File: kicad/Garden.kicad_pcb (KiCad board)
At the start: 2 copper layers, 13 parts, among them J1 Conn_01x03, J10 Conn_01x02, J2 Conn_01x03, J3 Conn_01x04, J4 Conn_01x06, J5 Conn_01x02, J6 Conn_01x02, J7 Conn_01x06, J8 Conn_01x03, J9 Conn_01x04

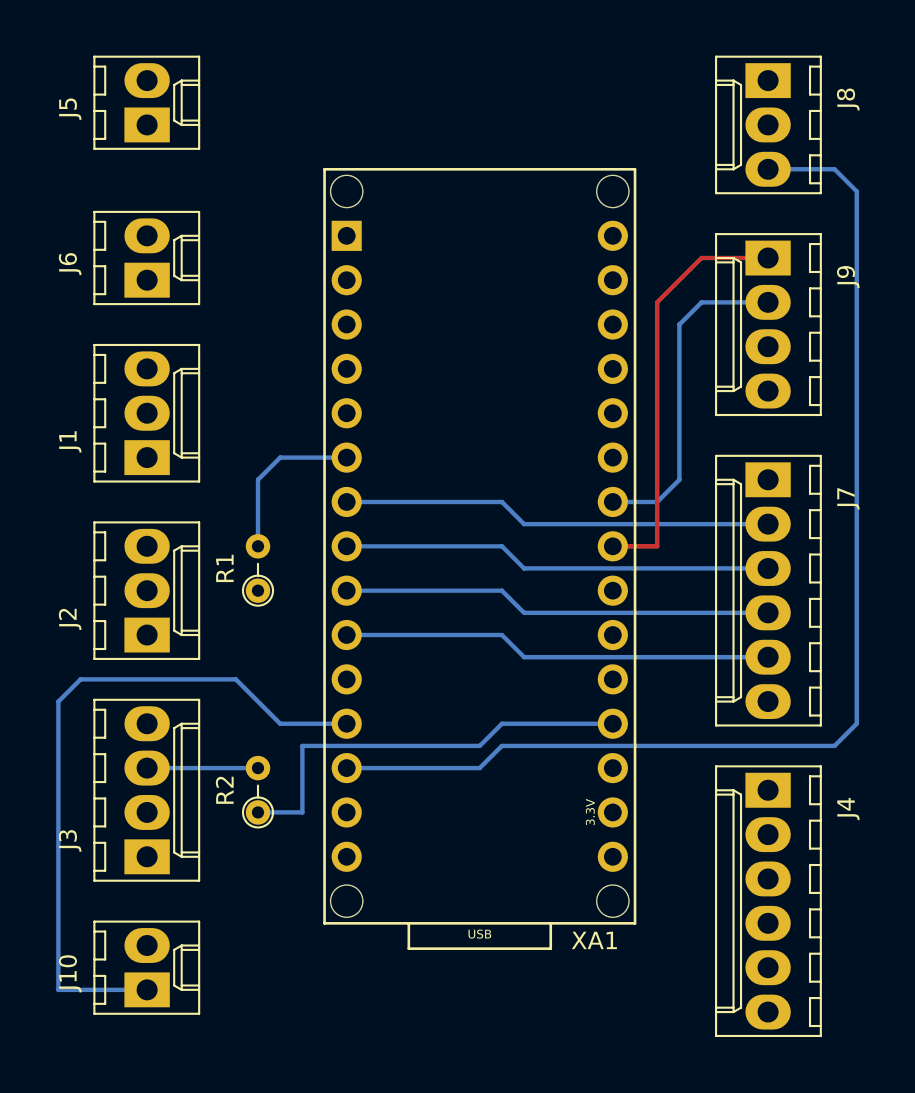
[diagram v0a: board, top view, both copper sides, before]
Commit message: Add connections for serial port to kicad files, add ground and +5V plane
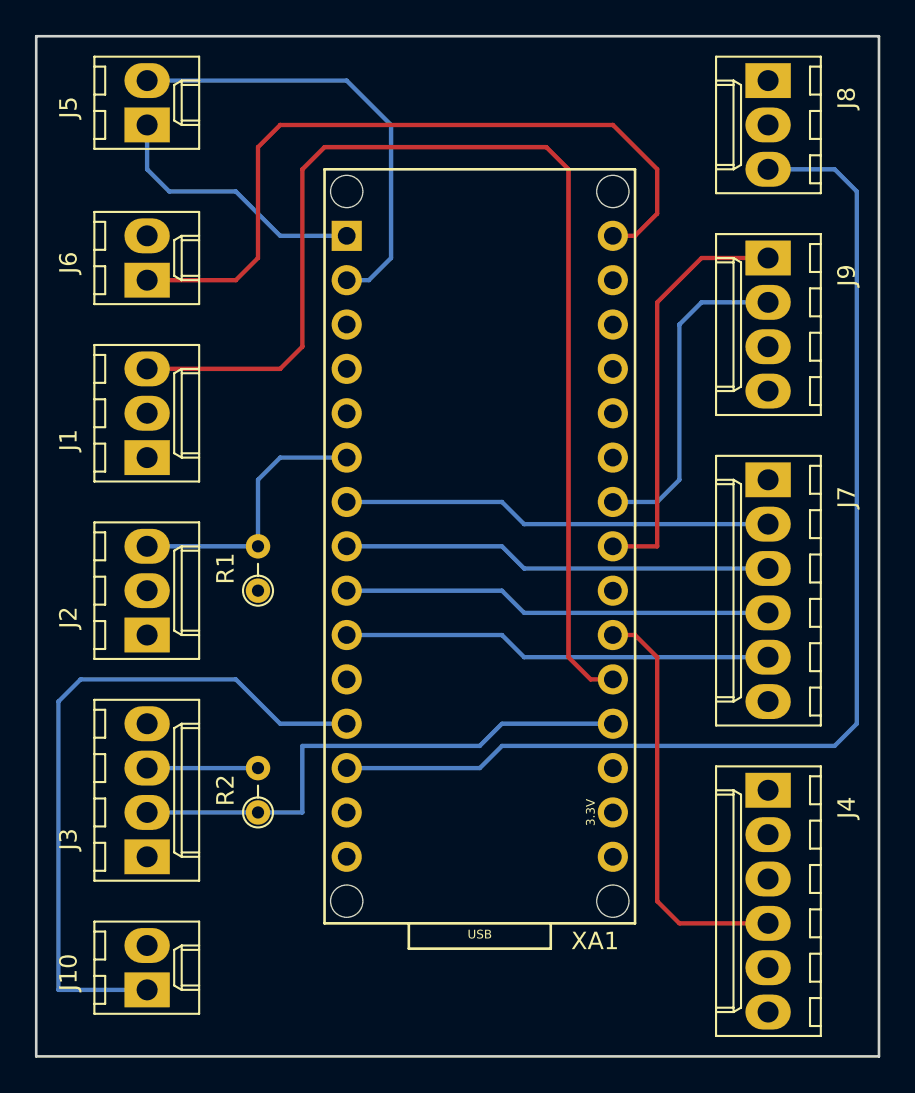
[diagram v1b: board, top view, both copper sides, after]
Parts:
- J1: value Conn_01x03 -> EC
- J10: value Conn_01x02 -> FAN_PWM
- J2: value Conn_01x03 -> TEMP
- J3: value Conn_01x04 -> DHT
- J4: value Conn_01x06 -> PH
- J5: value Conn_01x02 -> Serial
- J6: value Conn_01x02 -> Power
- J7: value Conn_01x06 -> RELAIS
- J8: value Conn_01x03 -> RC
- J9: value Conn_01x04 -> LCD
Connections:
- J4 pad 3: Net-(J4-Pad3) -> GND
- XA1 pad A1: Net-(XA1-PadA1) -> Net-(J1-Pad3)
- XA1 pad A2: Net-(XA1-PadA2) -> Net-(J4-Pad4)
- XA1 pad D0: Net-(XA1-PadD0) -> Net-(J5-Pad2)
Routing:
- net Net-(J1-Pad3): track 0.00 -> 66.9 mm
- net Net-(J6-Pad1): track 0.00 -> 43.3 mm
- net Net-(J5-Pad2): track 0.00 -> 25.7 mm
- net Net-(J4-Pad4): track 0.00 -> 23.9 mm
- net Net-(J5-Pad1): track 0.00 -> 15.5 mm
- net Net-(J3-Pad2): track 24.7 -> 31.0 mm
- net Net-(J2-Pad3): track 9.42 -> 15.8 mm
- added copper zone on F.Cu, net +5V
- added copper zone on B.Cu, net GND
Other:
- board outline added: 48.3 x 58.4 mm

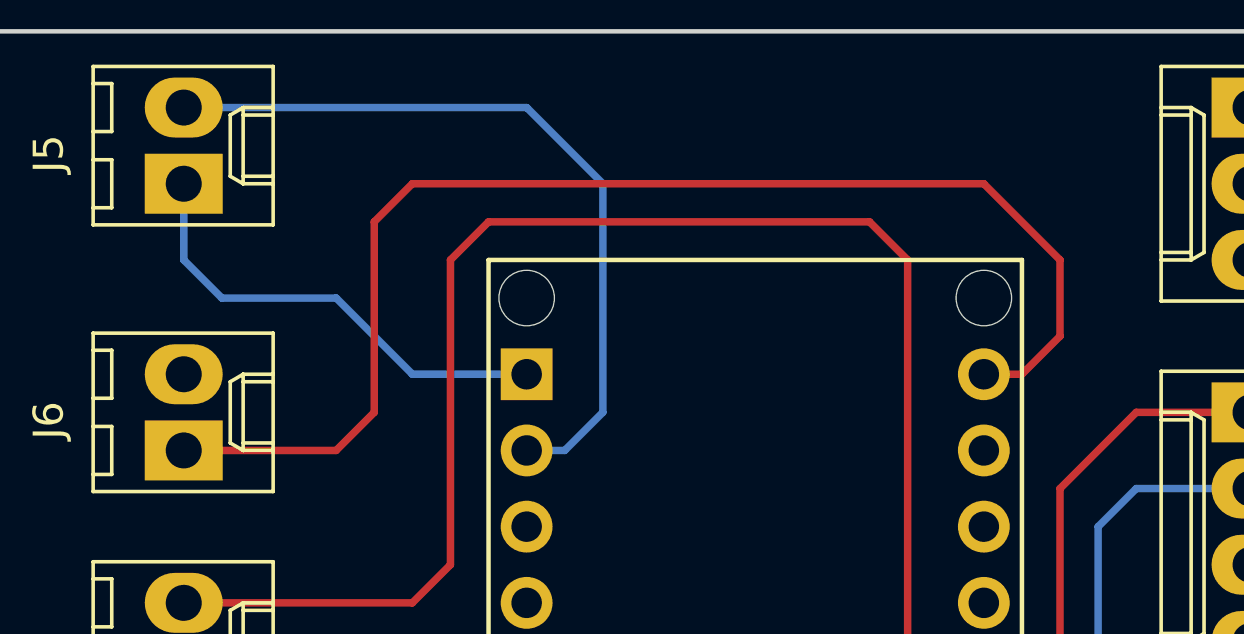
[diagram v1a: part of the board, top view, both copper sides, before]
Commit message: Clean up kicad schematic
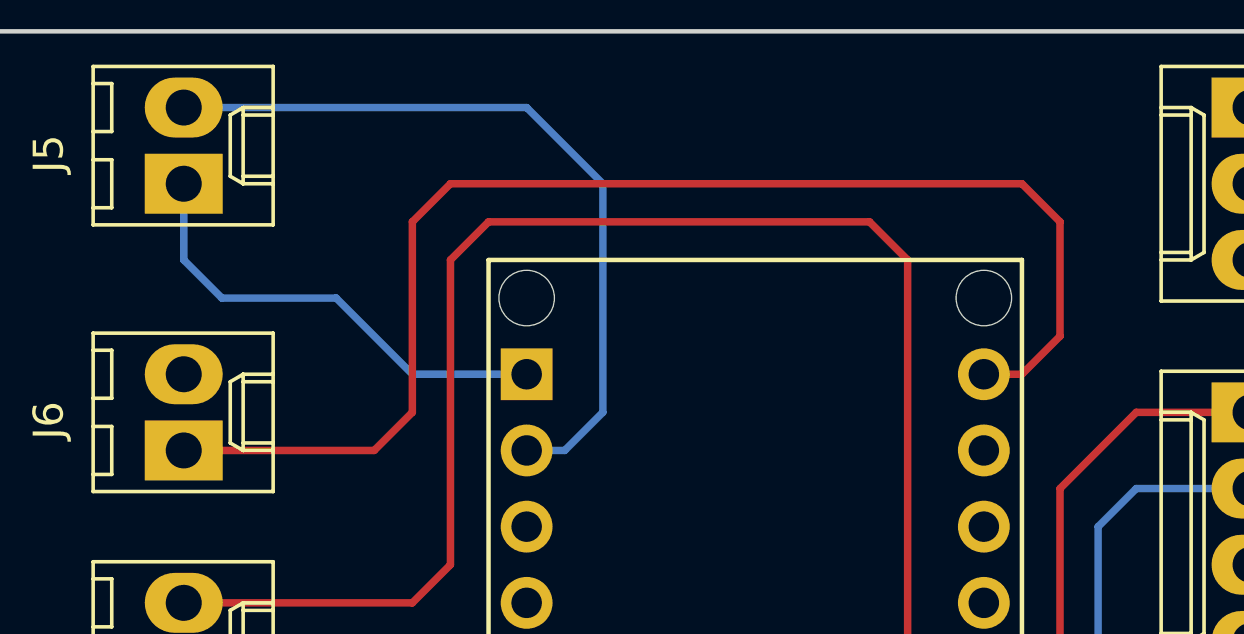
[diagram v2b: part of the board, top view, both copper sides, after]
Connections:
- net Net-(J1-Pad3) renamed A1
- net Net-(J10-Pad1) renamed D9
- net Net-(J2-Pad3) renamed D3
- net Net-(J3-Pad2) renamed A0
- net Net-(J4-Pad4) renamed A2
- net Net-(J5-Pad1) renamed TX
- net Net-(J5-Pad2) renamed RX
- net Net-(J6-Pad1) renamed VCC
- net Net-(J7-Pad2) renamed D4
- net Net-(J7-Pad3) renamed D5
- net Net-(J7-Pad4) renamed D6
- net Net-(J7-Pad5) renamed D7
- net Net-(J8-Pad3) renamed D10
- net Net-(J9-Pad1) renamed A4
- net Net-(J9-Pad2) renamed A5
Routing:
- net VCC: track 43.3 -> 44.0 mm

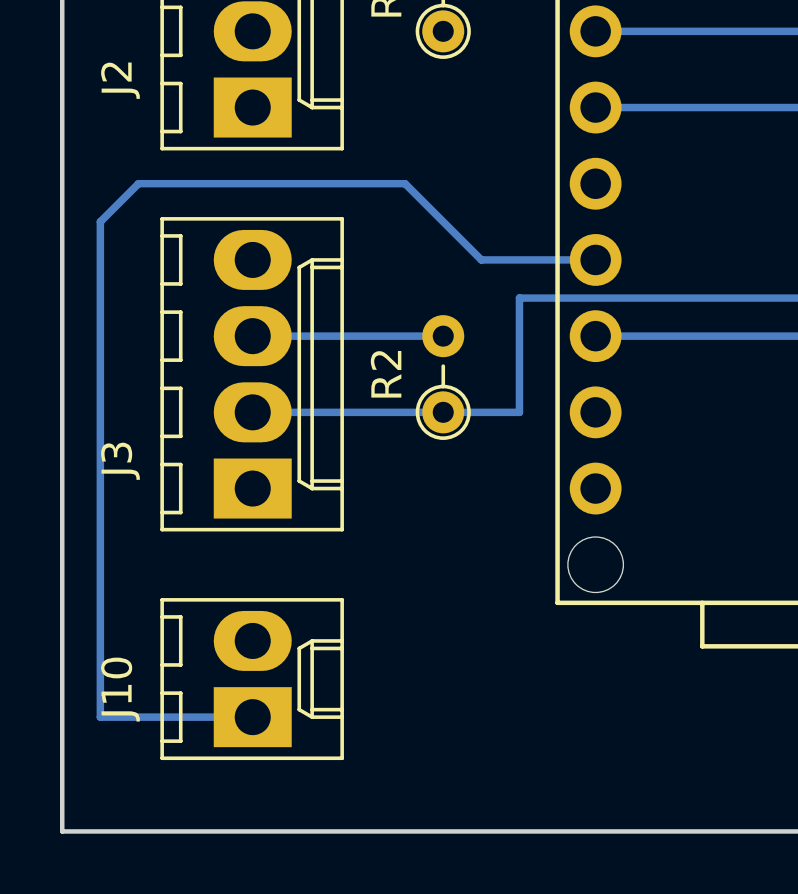
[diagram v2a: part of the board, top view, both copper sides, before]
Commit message: Fix unconnected planes
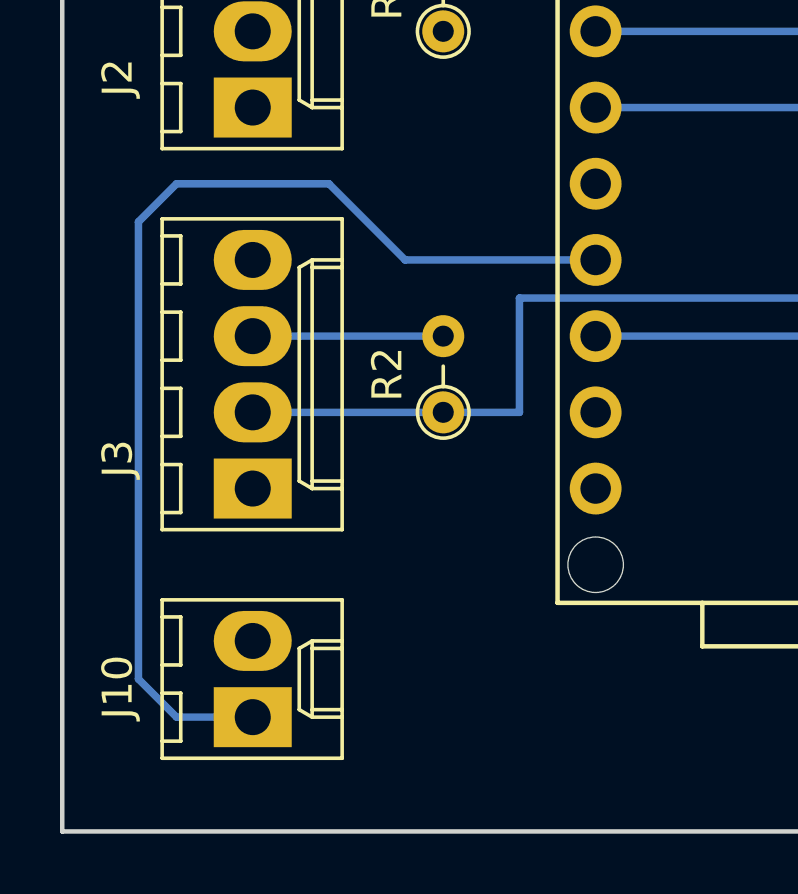
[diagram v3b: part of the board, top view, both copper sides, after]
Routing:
- net D9: track 39.7 -> 36.4 mm
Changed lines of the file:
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@@
   (general
     (links 37)
-    (no_connects 1)
+    (no_connects 0)
     (area 157.404999 78.664999 205.815001 137.235001)
     (thickness 1.6)
     (drawings 4)
-    (tracks 78)
+    (tracks 79)
     (zones 0)
     (modules 13)
@@
   (segment (start 194.31 104.14) (end 194.31 95.25) (width 0.25) (layer B.Cu) (net 31))
   (segment (start 193.04 105.41) (end 194.31 104.14) (width 0.25) (layer B.Cu) (net 31))
-  (segment (start 175.26 118.11) (end 171.45 118.11) (width 0.25) (layer B.Cu) (net 32))
-  (segment (start 158.75 133.35) (end 163.83 133.35) (width 0.25) (layer B.Cu) (net 32))
-  (segment (start 158.75 116.84) (end 158.75 133.35) (width 0.25) (layer B.Cu) (net 32))
-  (segment (start 160.02 115.57) (end 158.75 116.84) (width 0.25) (layer B.Cu) (net 32))
-  (segment (start 168.91 115.57) (end 160.02 115.57) (width 0.25) (layer B.Cu) (net 32))
-  (segment (start 171.45 118.11) (end 168.91 115.57) (width 0.25) (layer B.Cu) (net 32))
+  (segment (start 175.26 118.11) (end 168.91 118.11) (width 0.25) (layer B.Cu) (net 32))
+  (segment (start 161.29 133.35) (end 163.83 133.35) (width 0.25) (layer B.Cu) (net 32))
+  (segment (start 160.02 132.08) (end 161.29 133.35) (width 0.25) (layer B.Cu) (net 32))
+  (segment (start 160.02 116.84) (end 160.02 132.08) (width 0.25) (layer B.Cu) (net 32))
+  (segment (start 161.29 115.57) (end 160.02 116.84) (width 0.25) (layer B.Cu) (net 32))
+  (segment (start 166.37 115.57) (end 161.29 115.57) (width 0.25) (layer B.Cu) (net 32))
+  (segment (start 168.91 118.11) (end 166.37 115.57) (width 0.25) (layer B.Cu) (net 32))
   (zone (net 17) (net_name +5V) (layer F.Cu) (hatch edge 0.508)
     (connect_pads (clearance 0.508))

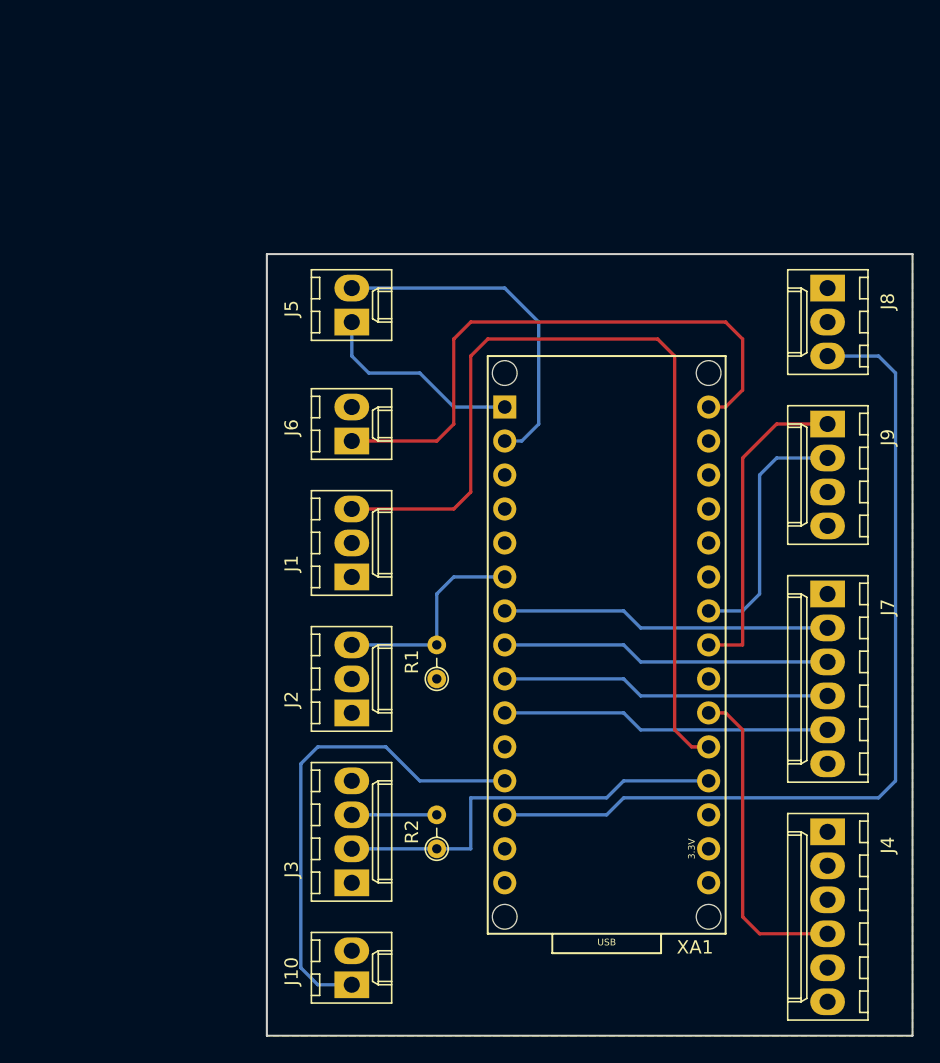
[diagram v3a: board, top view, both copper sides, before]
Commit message: Create Branch with buttons
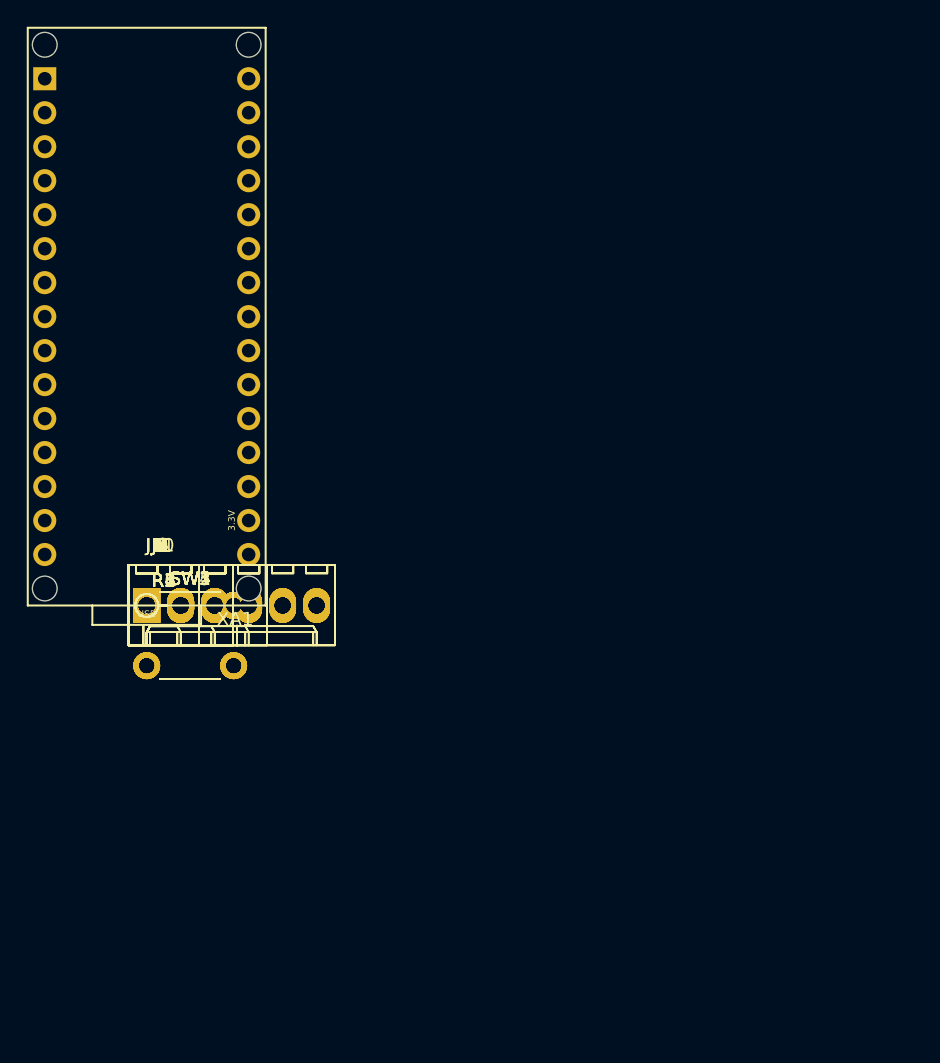
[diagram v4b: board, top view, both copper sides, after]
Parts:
- added J11: SPI, Connectors_Molex:Molex_KK-6410-06_06x2.54mm_Straight, F.Cu at (148.5, 105.0)
- added R3, R4, R5, R6, R7: R, Resistors_THT:R_Axial_DIN0204_L3.6mm_D1.6mm_P2.54mm_Vertical, F.Cu at (148.5, 105.0)
- added SW1, SW2, SW3, SW4, SW5: SW_Push, Buttons_Switches_THT:SW_PUSH_6mm, F.Cu at (148.5, 105.0)
- moved J8 56.1 mm to (148.5, 105.0), turned to 0 degrees
- moved J4 53.6 mm to (148.5, 105.0), turned to 0 degrees
- moved J9 52.7 mm to (148.5, 105.0), turned to 0 degrees
- moved J7 50.9 mm to (148.5, 105.0), turned to 0 degrees
- moved XA1 42.2 mm to (148.5, 105.0)
- moved J10 32.2 mm to (148.5, 105.0), turned to 0 degrees
- moved R2 28.3 mm to (148.5, 105.0), turned to 0 degrees
- moved J5 26.1 mm to (148.5, 105.0), turned to 0 degrees
- moved J3 25.8 mm to (148.5, 105.0), turned to 0 degrees
- moved R1 22.4 mm to (148.5, 105.0), turned to 0 degrees
- moved J6 19.6 mm to (148.5, 105.0), turned to 0 degrees
- moved J2 17.3 mm to (148.5, 105.0), turned to 0 degrees
- moved J1 15.5 mm to (148.5, 105.0), turned to 0 degrees
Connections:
- J8 pad 3: D10 -> D8
- XA1 pad D10: D10 -> D10_CS
- XA1 pad D11: Net-(XA1-PadD11) -> D11_MOSI
- XA1 pad D12: Net-(XA1-PadD12) -> D12_MISO
- XA1 pad D13: Net-(XA1-PadD13) -> D13_SCK
- XA1 pad D2: Net-(XA1-PadD2) -> D2
- XA1 pad D8: Net-(XA1-PadD8) -> D8
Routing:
- net A1: track 66.9 -> 0.00 mm
- net D10: track 66.3 -> 0.00 mm
- net VCC: track 44.0 -> 0.00 mm
- net D9: track 36.4 -> 0.00 mm
- net A0: track 31.0 -> 0.00 mm
- net RX: track 25.7 -> 0.00 mm
- net D6: track 24.7 -> 0.00 mm
- net D4: track 24.7 -> 0.00 mm
- net D7: track 24.7 -> 0.00 mm
- net D5: track 24.7 -> 0.00 mm
- net A2: track 23.9 -> 0.00 mm
- net A4: track 23.9 -> 0.00 mm
- net A5: track 18.8 -> 0.00 mm
- net D3: track 15.8 -> 0.00 mm
- net TX: track 15.5 -> 0.00 mm
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- removed copper zone on F.Cu, net +5V
- removed copper zone on B.Cu, net GND
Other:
- board outline removed
